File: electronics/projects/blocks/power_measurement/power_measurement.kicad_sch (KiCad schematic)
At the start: 4 parts, among them U401 PAC1934T-I/JQ

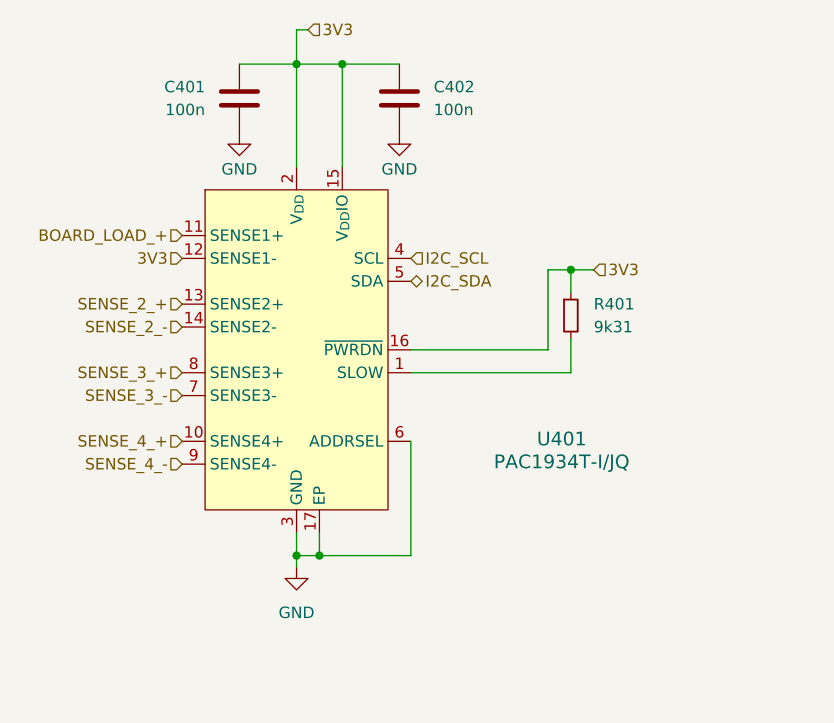
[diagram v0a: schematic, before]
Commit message: Create project to manage power measurement design block.
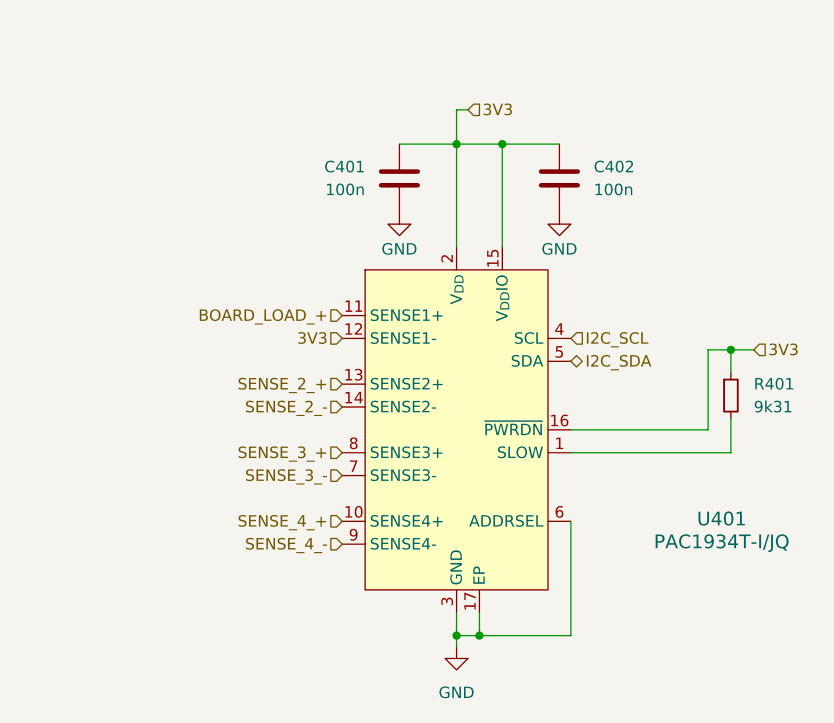
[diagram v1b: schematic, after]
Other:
- moved on the sheet: C401, C402, R401, U401

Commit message: Try another approach with design blocks. This approach annotates all components in the design block based around page number x 100, where the primary page for each design block starts at page 1.
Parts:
- renumbered C401 to C101, C402 to C102, R401 to R101, U401 to U101
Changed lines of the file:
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@@
 		(in_pos_files yes)
 		(dnp no)
-		(property "Reference" "U401"
+		(property "Reference" "U101"
 			(at 172.974 103.886 0)
 			(show_name no)
@@
 		)
 		(instances
-			(project "power_measurement"
-				(path "/00a61877-cce1-46a2-8791-e21dc4524eb1"
-					(reference "U401")
-					(unit 1)
-				)
-			)
 			(project "core_board"
 				(path "/695f882b-5312-4493-b26d-8f7d6768a9db/7b4bf28d-6031-4f39-baa2-3e9aecd97647"
@@
 			(project "power_measurement"
 				(path "/fa1a47ee-6efe-45dd-a018-8accaf81ef9e/b46f3a66-c5eb-49e8-b6df-1ac3fe8abb32"
-					(reference "U401")
+					(reference "U101")
 					(unit 1)
 				)
@@
 		(in_pos_files yes)
 		(dnp no)
-		(property "Reference" "#PWR0401"
+		(property "Reference" "#PWR0101"
 			(at 137.16 76.2 0)
 			(hide yes)
@@
 		)
 		(instances
-			(project "power_measurement"
-				(path "/00a61877-cce1-46a2-8791-e21dc4524eb1"
-					(reference "#PWR0401")
-					(unit 1)
-				)
-			)
 			(project "core_board"
 				(path "/695f882b-5312-4493-b26d-8f7d6768a9db/7b4bf28d-6031-4f39-baa2-3e9aecd97647"
@@
 			(project "power_measurement"
 				(path "/fa1a47ee-6efe-45dd-a018-8accaf81ef9e/b46f3a66-c5eb-49e8-b6df-1ac3fe8abb32"
-					(reference "#PWR0401")
+					(reference "#PWR0101")
 					(unit 1)
 				)
@@
 		(in_pos_files yes)
 		(dnp no)
-		(property "Reference" "C402"
+		(property "Reference" "C102"
 			(at 158.75 64.77 0)
 			(show_name no)
@@
 		)
 		(instances
-			(project "power_measurement"
-				(path "/00a61877-cce1-46a2-8791-e21dc4524eb1"
-					(reference "C402")
-					(unit 1)
-				)
-			)
 			(project "core_board"
 				(path "/695f882b-5312-4493-b26d-8f7d6768a9db/7b4bf28d-6031-4f39-baa2-3e9aecd97647"
@@
 			(project "power_measurement"
 				(path "/fa1a47ee-6efe-45dd-a018-8accaf81ef9e/b46f3a66-c5eb-49e8-b6df-1ac3fe8abb32"
-					(reference "C402")
+					(reference "C102")
 					(unit 1)
 				)
@@
 		(dnp no)
 		(fields_autoplaced yes)
-		(property "Reference" "R401"
+		(property "Reference" "R101"
 			(at 176.53 88.8999 0)
 			(show_name no)
@@
 		)
 		(instances
-			(project "power_measurement"
-				(path "/00a61877-cce1-46a2-8791-e21dc4524eb1"
-					(reference "R401")
-					(unit 1)
-				)
-			)
 			(project "core_board"
 				(path "/695f882b-5312-4493-b26d-8f7d6768a9db/7b4bf28d-6031-4f39-baa2-3e9aecd97647"
@@
 			(project "power_measurement"
 				(path "/fa1a47ee-6efe-45dd-a018-8accaf81ef9e/b46f3a66-c5eb-49e8-b6df-1ac3fe8abb32"
-					(reference "R401")
+					(reference "R101")
 					(unit 1)
 				)
@@
 		(in_pos_files yes)
 		(dnp no)
-		(property "Reference" "#PWR0403"
+		(property "Reference" "#PWR0103"
 			(at 154.94 76.2 0)
 			(hide yes)
@@
 		)
 		(instances
-			(project "power_measurement"
-				(path "/00a61877-cce1-46a2-8791-e21dc4524eb1"
-					(reference "#PWR0403")
-					(unit 1)
-				)
-			)
 			(project "core_board"
 				(path "/695f882b-5312-4493-b26d-8f7d6768a9db/7b4bf28d-6031-4f39-baa2-3e9aecd97647"
@@
 			(project "power_measurement"
 				(path "/fa1a47ee-6efe-45dd-a018-8accaf81ef9e/b46f3a66-c5eb-49e8-b6df-1ac3fe8abb32"
-					(reference "#PWR0403")
+					(reference "#PWR0103")
 					(unit 1)
 				)
@@
 		(dnp no)
 		(fields_autoplaced yes)
-		(property "Reference" "C401"
+		(property "Reference" "C101"
 			(at 133.35 64.77 0)
 			(show_name no)
@@
 		)
 		(instances
-			(project "power_measurement"
-				(path "/00a61877-cce1-46a2-8791-e21dc4524eb1"
-					(reference "C401")
-					(unit 1)
-				)
-			)
 			(project "core_board"
 				(path "/695f882b-5312-4493-b26d-8f7d6768a9db/7b4bf28d-6031-4f39-baa2-3e9aecd97647"
@@
 			(project "power_measurement"
 				(path "/fa1a47ee-6efe-45dd-a018-8accaf81ef9e/b46f3a66-c5eb-49e8-b6df-1ac3fe8abb32"
-					(reference "C401")
+					(reference "C101")
 					(unit 1)
 				)
@@
 		(dnp no)
 		(fields_autoplaced yes)
-		(property "Reference" "#PWR0402"
+		(property "Reference" "#PWR0102"
 			(at 143.51 124.46 0)
 			(hide yes)
@@
 		)
 		(instances
-			(project "power_measurement"
-				(path "/00a61877-cce1-46a2-8791-e21dc4524eb1"
-					(reference "#PWR0402")
-					(unit 1)
-				)
-			)
 			(project "core_board"
 				(path "/695f882b-5312-4493-b26d-8f7d6768a9db/7b4bf28d-6031-4f39-baa2-3e9aecd97647"
@@
 			(project "power_measurement"
 				(path "/fa1a47ee-6efe-45dd-a018-8accaf81ef9e/b46f3a66-c5eb-49e8-b6df-1ac3fe8abb32"
-					(reference "#PWR0402")
-					(unit 1)
-				)
+					(reference "#PWR0102")
+					(unit 1)
+				)
